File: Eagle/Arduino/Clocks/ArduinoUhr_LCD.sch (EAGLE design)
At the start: 13 parts

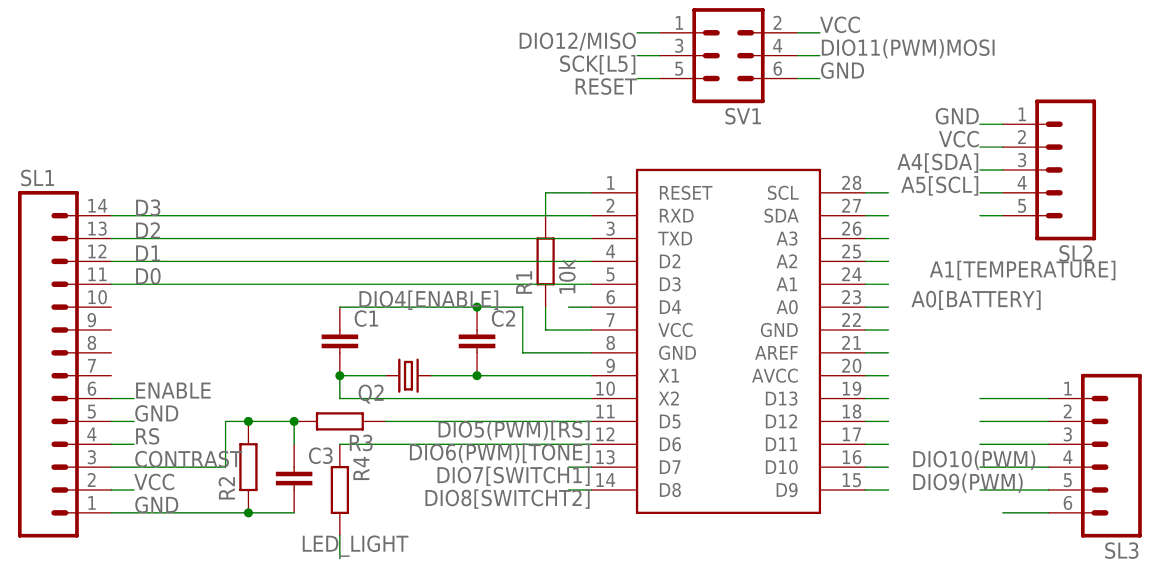
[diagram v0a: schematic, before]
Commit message: changed layout for new LCD Display
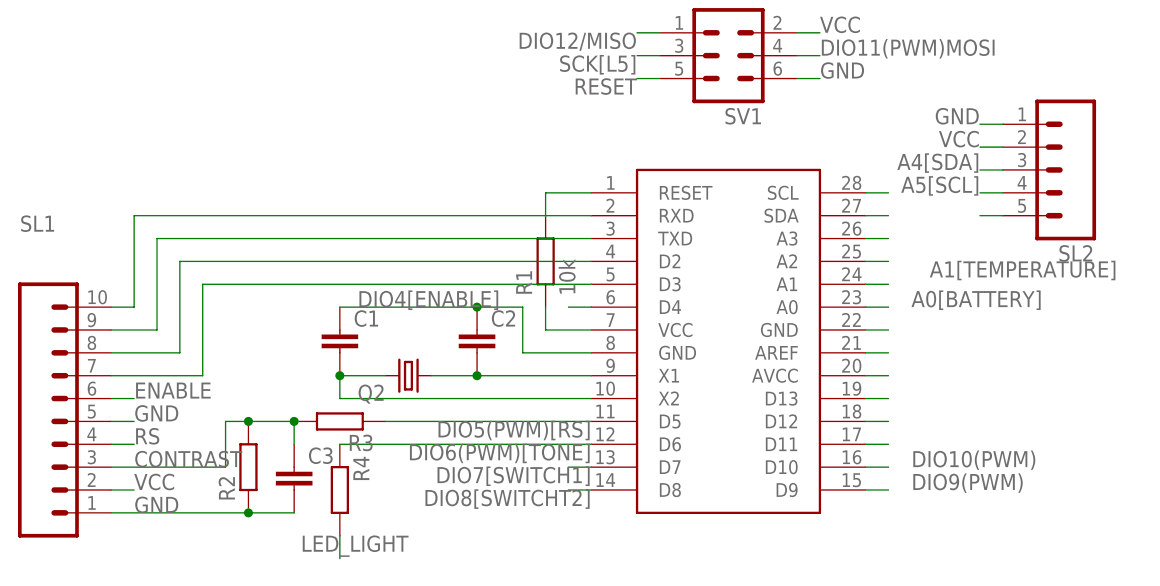
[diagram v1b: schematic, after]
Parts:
- removed SL3: (no value), con-amp-quick:M06
- SL1: device con-amp-quick:M14 -> con-amp-quick:M10
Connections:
- removed net D0: SL1.11, U$1.D3
- removed net D1: SL1.12, U$1.D2
- removed net D2: SL1.13, U$1.TXD
- removed net D3: SL1.14, U$1.RXD
- new net N$1: SL1.10, U$1.RXD
- new net N$2: SL1.9, U$1.TXD
- new net N$3: SL1.8, U$1.D2
- new net N$4: SL1.7, U$1.D3
- net DIO10(PWM): no longer SL3.4
- net DIO11(PWM)MOSI: no longer SL3.3
- net DIO12/MISO: no longer SL3.2
- net DIO9(PWM): no longer SL3.5
- net GND: no longer SL3.6
- net SCK[L5]: no longer SL3.1

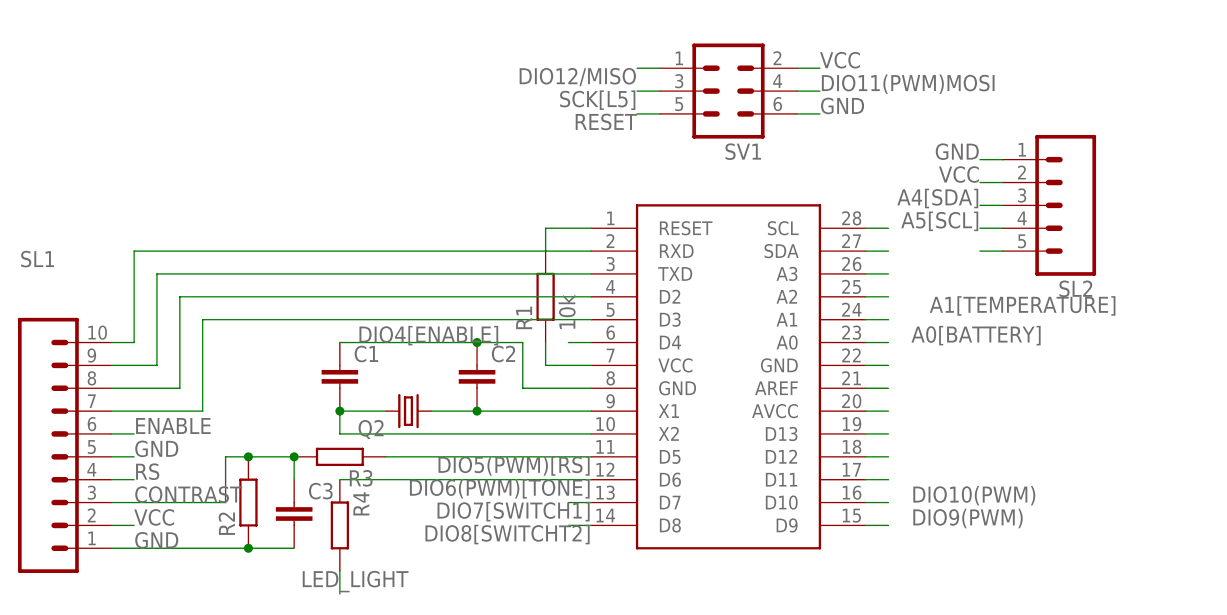
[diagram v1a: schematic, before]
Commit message: Changes for severals files
bugfixes, pins changed
 - Arduino/Sketches/Uhren/ClockWithTimers/clockwithtimers/SettingStates.cpp
 - Arduino/Sketches/Uhren/ClockWithTimers/clockwithtimers/big_ben.h
 - Arduino/Sketches/Uhren/ClockWithTimers/clockwithtimers/clockwithtimers.ino
 - Arduino/Sketches/Uhren/ClockWithTimers/clockwithtimers/ioAt328.h
 - Arduino/Sketches/Uhren/ClockWithTimers/clockwithtimers/ioMega2560.h
bugfixes, and comments
 - Arduino/libraries/Melody/examples/melody_play/melody_play.ino
 - Arduino/libraries/Melody/keywords.txt
 - Arduino/libraries/Melody/library.properties
 - Arduino/libraries/Melody/src/Melody.h
Layout for arduino pins changed
 - Eagle/Arduino/Clocks/ArduinoUhr_LCD.brd
 - Eagle/Arduino/Clocks/ArduinoUhr_LCD.sch
Added a thread for arduino loop
 - Qt/ArduinoUnittest/ArduinoUnittest/ArduinoUnittest.pro
 - Qt/ArduinoUnittest/ArduinoUnittest/arduinoworker.cpp
 - Qt/ArduinoUnittest/ArduinoUnittest/arduinoworker.h
 - Qt/ArduinoUnittest/ArduinoUnittest/mainwindow.cpp
 - Qt/ArduinoUnittest/ArduinoUnittest/mainwindow.h
bugfix
 - Qt/SerialCommunicator/SerialCommunicator/mainwindow.cpp
 - Qt/SerialCommunicator/SerialCommunicator/pincommon.h
c++17 fallthrough for code clarity
 - Qt/acalc/src/acalc.pro
 - Qt/acalc/src/carithmetic.cpp
 - Qt/acalc/src/carithmetic.h
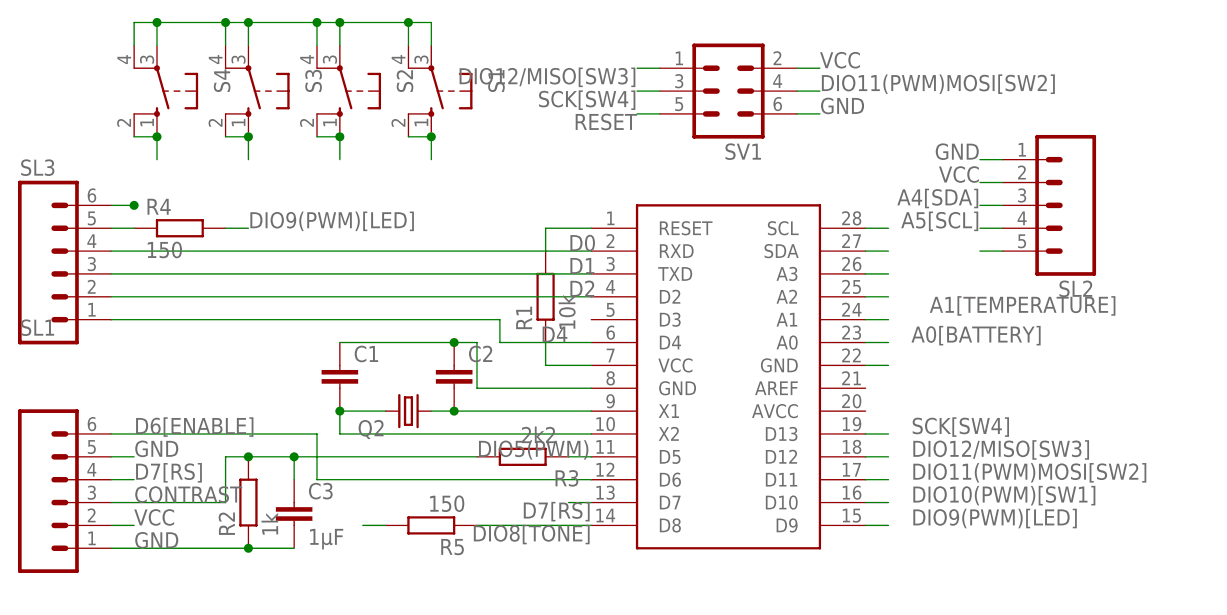
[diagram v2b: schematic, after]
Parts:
- added R5: 150, rcl:R-EU_0204/7
- added S1, S2, S3, S4: (no value), switch-omron:10-XX
- added SL3: (no value), con-amp-quick:M06
- C3: value (none) -> 1µF
- R2: value (none) -> 1k
- R3: value (none) -> 2k2
- R4: value (none) -> 150; device rcl:R-EU_0204/7 -> resistor:R-EU_0207/10
- SL1: device con-amp-quick:M10 -> con-amp-quick:M06
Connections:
- net DIO5(PWM)[RS] renamed DIO5(PWM)
- removed net AREF: U$1.AREF
- removed net DIO10(PWM): U$1.D10
- removed net DIO11(PWM)MOSI: SV1.4, U$1.D11
- removed net DIO12/MISO: SV1.1, U$1.D12
- removed net DIO4[ENABLE]: U$1.D4
- removed net DIO6(PWM)[TONE]: R4.1, U$1.D6
- removed net DIO7[SWITCH1]: U$1.D7
- removed net DIO8[SWITCHT2]: U$1.D8
- removed net DIO9(PWM): U$1.D9
- removed net ENABLE: SL1.6
- removed net LED_LIGHT: R4.2
- removed net N$1: SL1.10, U$1.RXD
- removed net N$4: SL1.7, U$1.D3
- removed net RS: SL1.4
- removed net SCK[L5]: SV1.3, U$1.D13
- new net D0: SL3.4, U$1.RXD
- new net D1: SL3.3, U$1.TXD
- new net D2: SL3.2, U$1.D2
- new net D4: SL3.1, U$1.D4
- new net D6[ENABLE]: SL1.6, U$1.D6
- new net D7[RS]: SL1.4, U$1.D7
- new net DIO10(PWM)[SW1]: S4.S, S4.S1, U$1.D10
- new net DIO11(PWM)MOSI[SW2]: S3.S, S3.S1, SV1.4, U$1.D11
- new net DIO12/MISO[SW3]: S2.S, S2.S1, SV1.1, U$1.D12
- new net DIO8[TONE]: R5.1, U$1.D8
- new net DIO9(PWM)[LED]: R4.2, U$1.D9
- new net SCK[SW4]: S1.S, S1.S1, SV1.3, U$1.D13
- net GND: now also S1.P, S1.P1, S2.P, S2.P1, S3.P, S3.P1, S4.P, S4.P1, SL3.6
- net N$2: now also R4.1, SL3.5; no longer SL1.9, U$1.TXD
- net N$3: now also R5.2; no longer SL1.8, U$1.D2
- net VCC: no longer U$1.AVCC
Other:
- moved on the sheet: C2, R3, R4

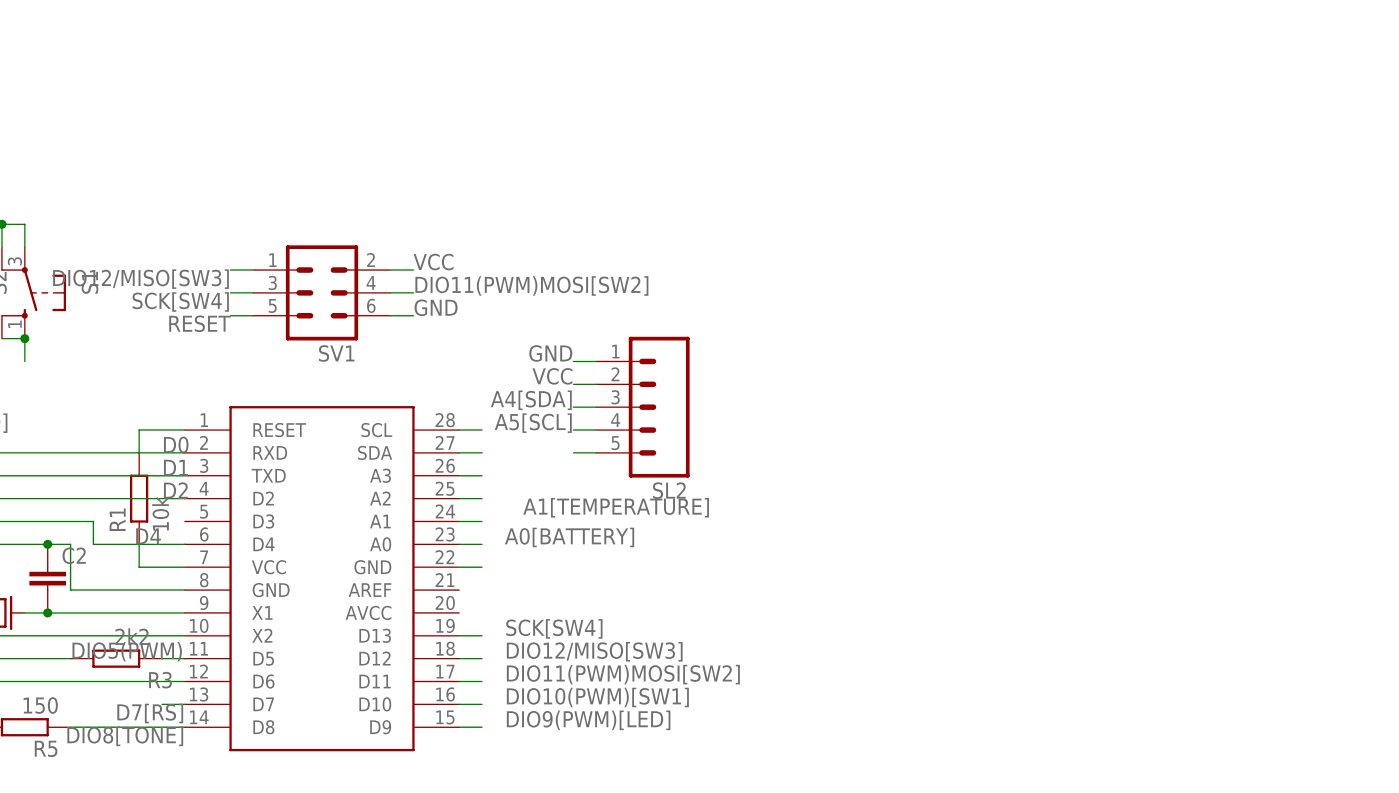
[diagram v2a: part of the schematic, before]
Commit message: added language selection and usb current measurement
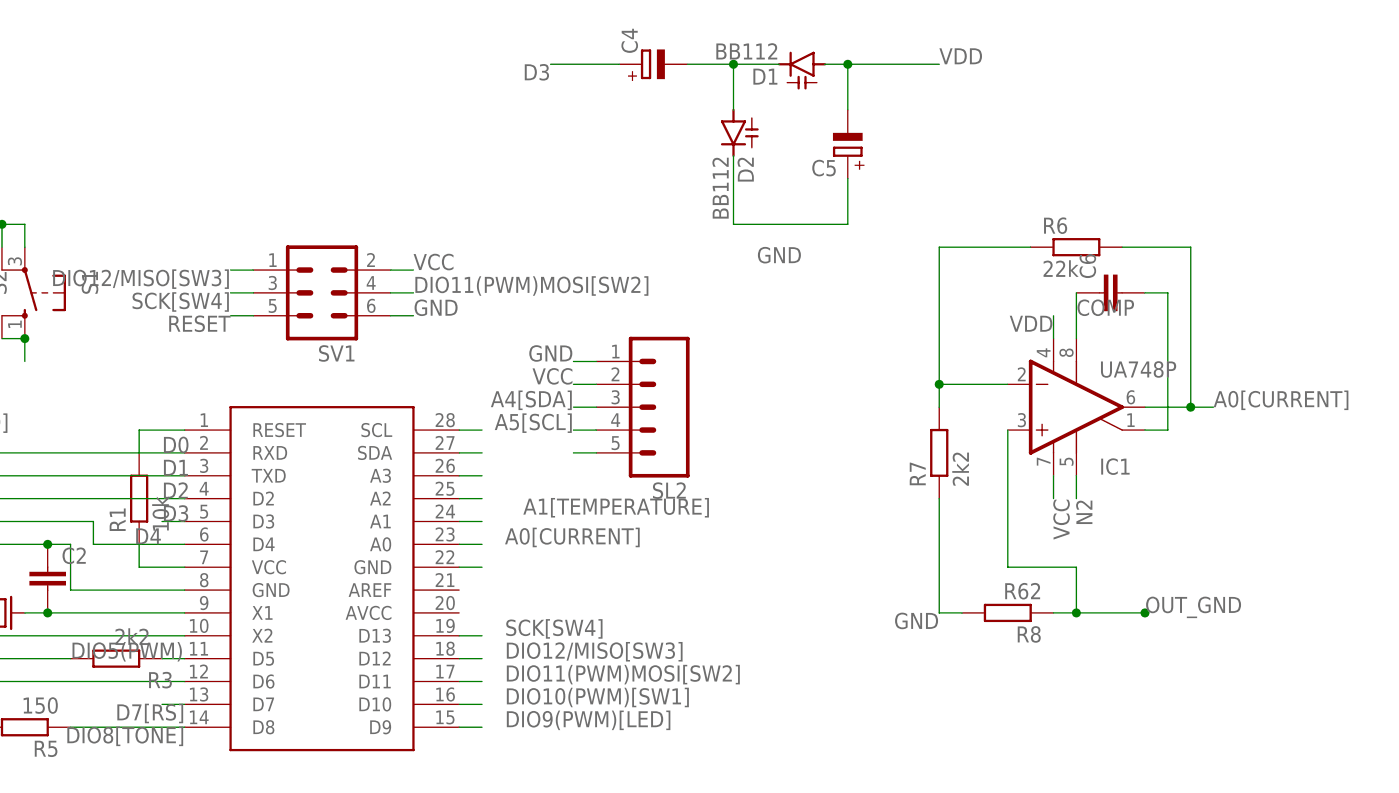
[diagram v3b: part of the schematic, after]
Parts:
- added C4, C5: (no value), rcl:CPOL-EUE2.5-5
- added C6: (no value), rcl:C-EU025-024X044
- added D1, D2: BB112, diode:BB112
- added IC1: UA748P, linear:UA748P
- added R6: 22k, rcl:R-EU_0207/12
- added R7: 2k2, rcl:R-EU_0207/12
- added R8: R62, rcl:R-EU_0207/12
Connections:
- removed net A0[BATTERY]: U$1.A0
- new net A0[CURRENT]: IC1.OUT, R6.2, U$1.A0
- new net COMP: C6.1, IC1.CMP
- new net D3: C4.+, U$1.D3
- new net N$1: C4.-, D1.C, D2.A
- new net N$4: C6.2, IC1.ON/CMP
- new net N$5: IC1.-IN, R6.1, R7.2
- new net N2: IC1.ON
- new net OUT_GND: IC1.+IN, R8.1
- new net VDD: C5.-, D1.A, IC1.V-
- net GND: now also C5.+, D2.C, R7.1, R8.2
- net VCC: now also IC1.V+

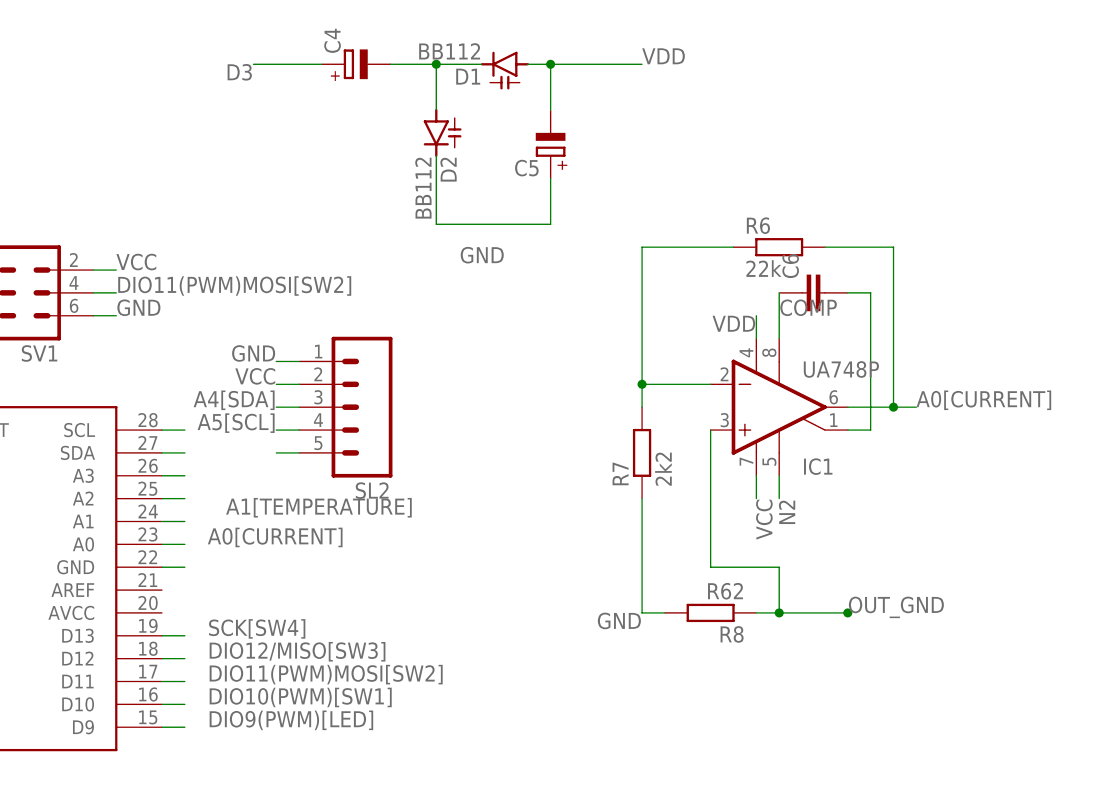
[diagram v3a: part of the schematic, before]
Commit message: changed schematics - Measurement of current
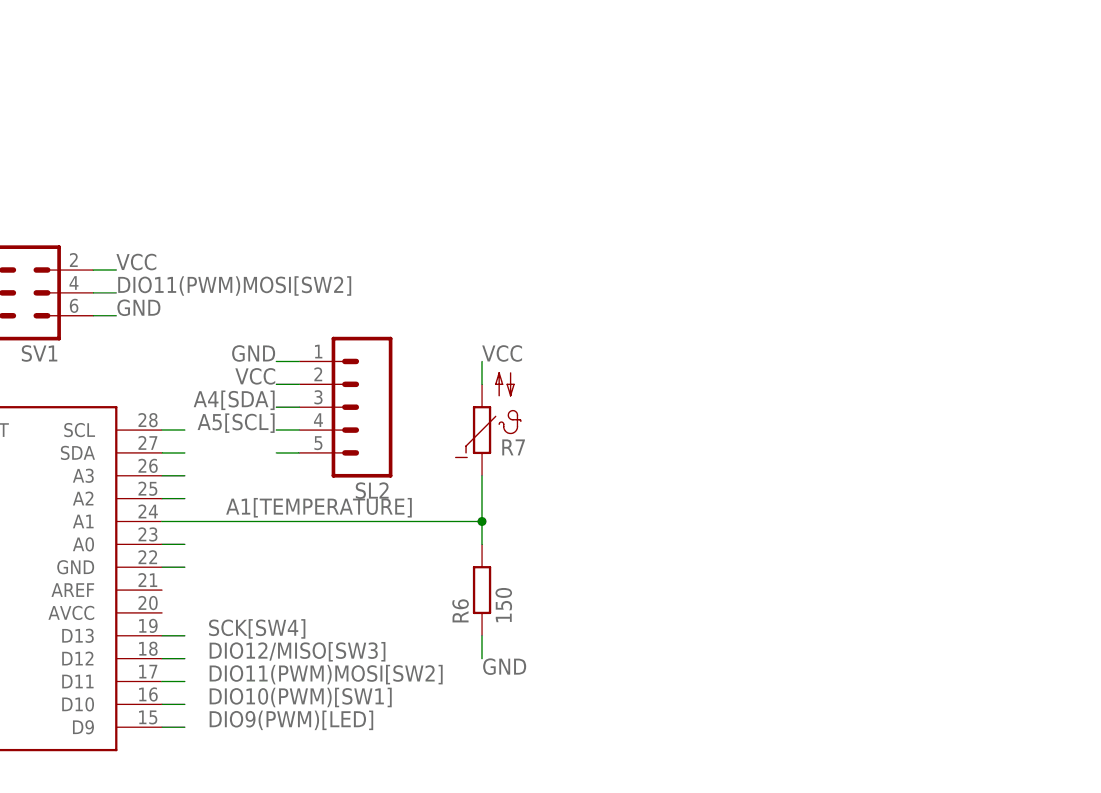
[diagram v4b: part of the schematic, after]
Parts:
- removed C4, C5: (no value), rcl:CPOL-EUE2.5-5
- removed C6: (no value), rcl:C-EU025-024X044
- removed D1, D2: BB112, diode:BB112
- removed IC1: UA748P, linear:UA748P
- removed R8: R62, rcl:R-EU_0207/12
- R6: value 22k -> 150; device rcl:R-EU_0207/12 -> resistor:R-EU_0207/10
- R7: value 2k2 -> (none); device rcl:R-EU_0207/12 -> ptc-ntc:NTC640-9
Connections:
- removed net COMP: C6.1, IC1.CMP
- removed net N$1: C4.-, D1.C, D2.A
- removed net N$4: C6.2, IC1.ON/CMP
- removed net N$5: IC1.-IN, R6.1, R7.2
- removed net N2: IC1.ON
- removed net OUT_GND: IC1.+IN, R8.1
- removed net VDD: C5.-, D1.A, IC1.V-
- net A0[CURRENT]: no longer IC1.OUT, R6.2
- net A1[TEMPERATURE]: now also R6.2, R7.1
- net D3: no longer C4.+
- net GND: now also R6.1; no longer C5.+, D2.C, R7.1, R8.2
- net VCC: now also R7.2; no longer IC1.V+
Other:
- moved on the sheet: R6
